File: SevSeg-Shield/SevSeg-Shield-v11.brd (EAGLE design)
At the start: 59.7 x 53.3 mm, 5 parts, among them U2 ARDUINO_SHIELD

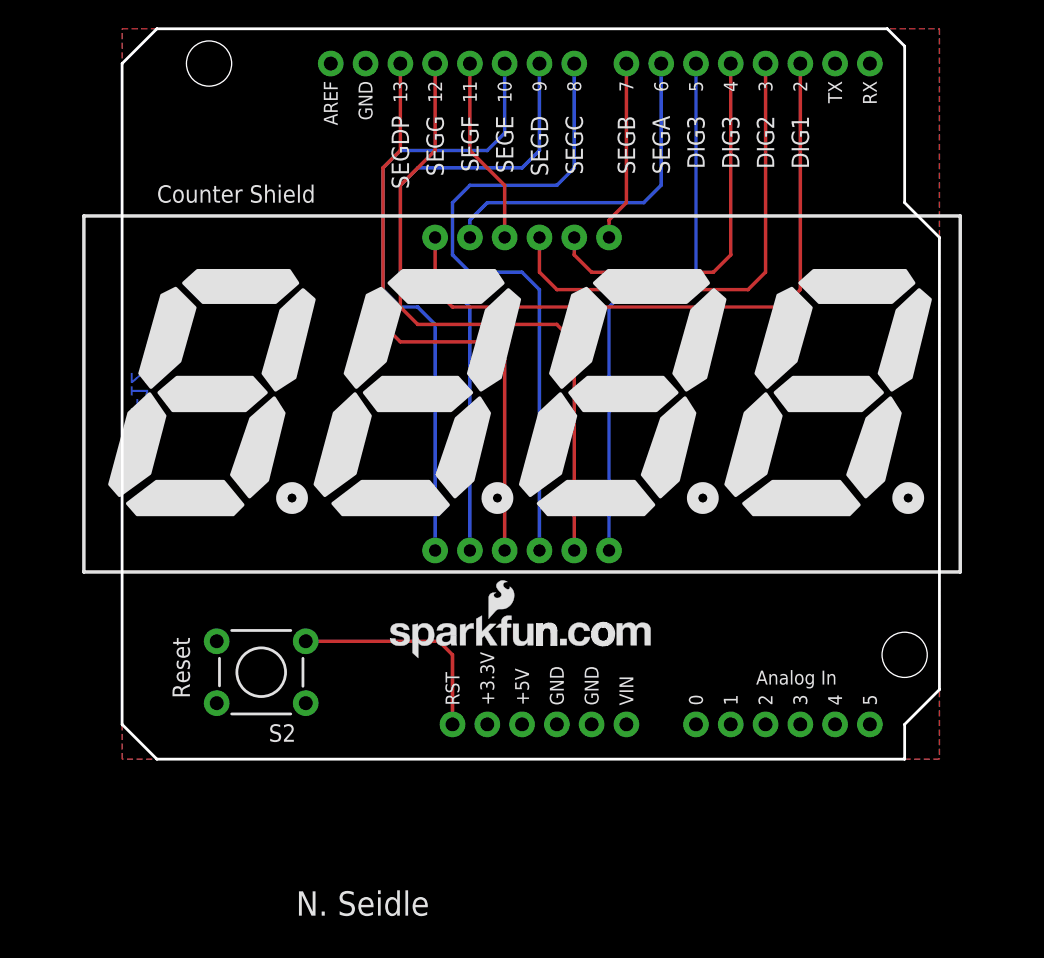
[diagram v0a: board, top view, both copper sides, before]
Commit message: Updated the footprint of the display.
Proto worked but the footprint was not quite right. This version should
work a lot better.
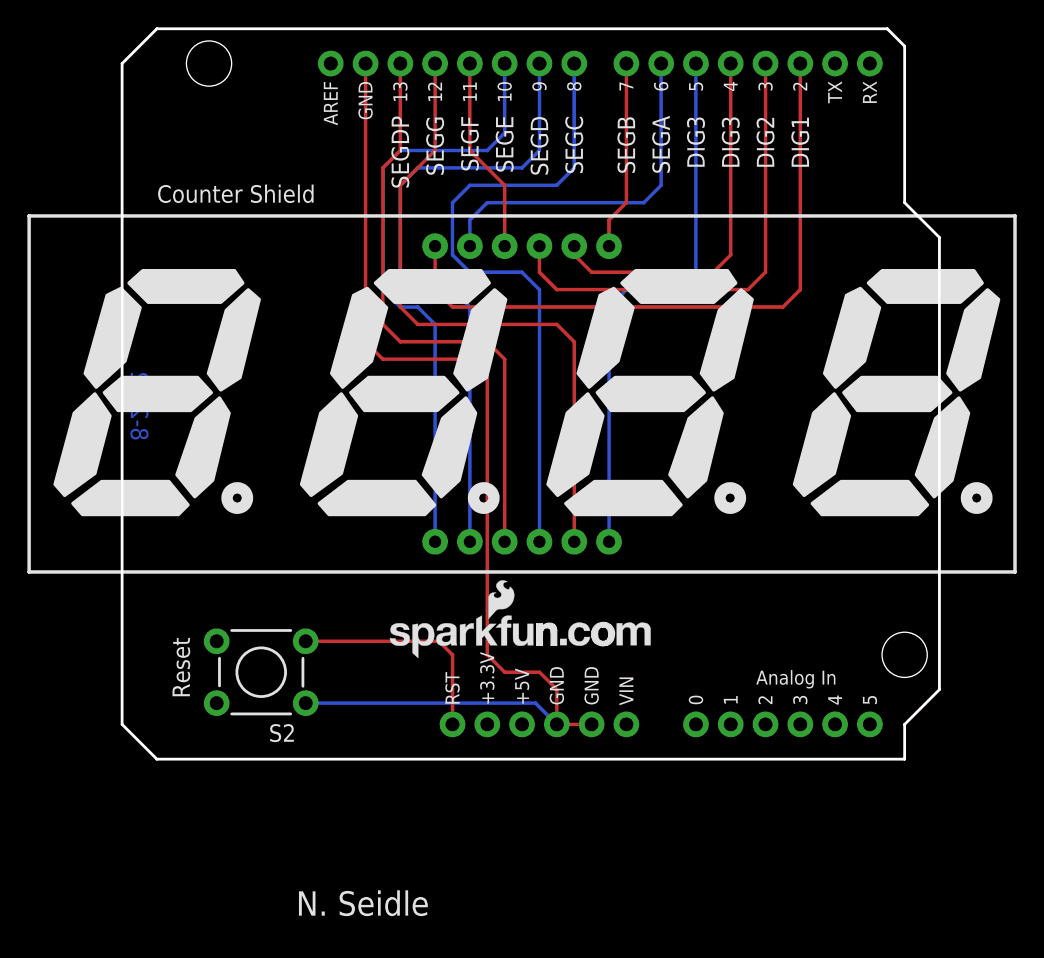
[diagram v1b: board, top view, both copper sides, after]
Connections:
- removed net VCC: U2.5V
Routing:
- net GND: track 0.00 -> 80.8 mm
- net SEGDP: track 43.5 -> 42.9 mm
- net SEGG: track 47.8 -> 47.2 mm
- net SEGF: track 13.8 -> 14.4 mm
- net SEGC: track 47.8 -> 47.2 mm
- net SEGB: track 13.2 -> 13.9 mm
- net SEGA: track 25.2 -> 25.8 mm
- net DIG3: track 27.7 -> 27.1 mm
- net DIG2: track 35.3 -> 34.7 mm
- net DIG1: track 48.0 -> 47.4 mm
- net SEGE: track 45.3 -> 44.6 mm
- net SEGD: track 47.8 -> 47.2 mm
- net DIG4: track 40.4 -> 39.8 mm
- removed copper zone on layer 1, net GND
- removed copper zone on layer 16, net GND
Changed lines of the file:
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@@
 <layer number="18" name="Vias" color="2" fill="1" visible="yes" active="yes"/>
 <layer number="19" name="Unrouted" color="6" fill="1" visible="yes" active="yes"/>
-<layer number="20" name="Dimension" color="6" fill="1" visible="yes" active="yes"/>
+<layer number="20" name="Dimension" color="24" fill="1" visible="yes" active="yes"/>
 <layer number="21" name="tPlace" color="16" fill="1" visible="yes" active="yes"/>
 <layer number="22" name="bPlace" color="14" fill="1" visible="yes" active="yes"/>
@@
 <contactref element="U2" pad="GND@0"/>
 <contactref element="S2" pad="1"/>
-<polygon width="0.2032" layer="1" isolate="0.3048">
-<vertex x="59.69" y="53.34"/>
-<vertex x="59.69" y="0"/>
-<vertex x="0" y="0"/>
-<vertex x="0" y="53.34"/>
-</polygon>
-<polygon width="0.2032" layer="16" isolate="0.3048">
-<vertex x="0" y="53.34"/>
-<vertex x="59.69" y="53.34"/>
-<vertex x="59.69" y="0"/>
-<vertex x="0" y="0"/>
-</polygon>
-</signal>
-<signal name="VCC">
-<contactref element="U2" pad="5V"/>
+<wire x1="17.78" y1="50.8" x2="17.78" y2="30.48" width="0.254" layer="1"/>
+<wire x1="17.78" y1="30.48" x2="19.05" y2="29.21" width="0.254" layer="1"/>
+<wire x1="19.05" y1="29.21" x2="25.4" y2="29.21" width="0.254" layer="1"/>
+<wire x1="25.4" y1="29.21" x2="26.67" y2="27.94" width="0.254" layer="1"/>
+<wire x1="26.67" y1="27.94" x2="26.67" y2="7.62" width="0.254" layer="1"/>
+<wire x1="26.67" y1="7.62" x2="27.94" y2="6.35" width="0.254" layer="1"/>
+<wire x1="27.94" y1="6.35" x2="30.48" y2="6.35" width="0.254" layer="1"/>
+<wire x1="30.48" y1="6.35" x2="31.75" y2="5.08" width="0.254" layer="1"/>
+<wire x1="31.75" y1="5.08" x2="31.75" y2="2.54" width="0.254" layer="1"/>
+<wire x1="13.4112" y1="4.0894" x2="30.2006" y2="4.0894" width="0.254" layer="16"/>
+<wire x1="30.2006" y1="4.0894" x2="31.75" y2="2.54" width="0.254" layer="16"/>
+<wire x1="34.29" y1="2.54" x2="31.75" y2="2.54" width="0.254" layer="1"/>
 </signal>
 <signal name="ARST">
@@
 <wire x1="48.26" y1="33.02" x2="24.13" y2="33.02" width="0.254" layer="1"/>
 <wire x1="24.13" y1="33.02" x2="22.86" y2="34.29" width="0.254" layer="1"/>
-<wire x1="22.86" y1="34.29" x2="22.86" y2="38.1" width="0.254" layer="1"/>
+<wire x1="22.86" y1="34.29" x2="22.86" y2="37.465" width="0.254" layer="1"/>
 </signal>
 <signal name="DIG2">
 <contactref element="U$1" pad="9"/>
 <contactref element="U2" pad="D3"/>
-<wire x1="30.48" y1="38.1" x2="30.48" y2="35.56" width="0.254" layer="1"/>
+<wire x1="30.48" y1="37.465" x2="30.48" y2="35.56" width="0.254" layer="1"/>
 <wire x1="30.48" y1="35.56" x2="31.75" y2="34.29" width="0.254" layer="1"/>
 <wire x1="31.75" y1="34.29" x2="45.72" y2="34.29" width="0.254" layer="1"/>
@@
 <contactref element="U$1" pad="8"/>
 <contactref element="U2" pad="D4"/>
-<wire x1="33.02" y1="38.1" x2="33.02" y2="36.83" width="0.254" layer="1"/>
+<wire x1="33.02" y1="37.465" x2="33.02" y2="36.83" width="0.254" layer="1"/>
 <wire x1="33.02" y1="36.83" x2="34.29" y2="35.56" width="0.254" layer="1"/>
 <wire x1="34.29" y1="35.56" x2="43.18" y2="35.56" width="0.254" layer="1"/>
@@
 <contactref element="U$1" pad="6"/>
 <contactref element="U2" pad="D5"/>
-<wire x1="35.56" y1="15.24" x2="35.56" y2="33.02" width="0.254" layer="16"/>
+<wire x1="35.56" y1="15.875" x2="35.56" y2="33.02" width="0.254" layer="16"/>
 <wire x1="35.56" y1="33.02" x2="36.83" y2="34.29" width="0.254" layer="16"/>
 <wire x1="36.83" y1="34.29" x2="40.64" y2="34.29" width="0.254" layer="16"/>
@@
 <contactref element="U$1" pad="3"/>
 <contactref element="U2" pad="D13"/>
-<wire x1="27.94" y1="15.24" x2="27.94" y2="29.21" width="0.254" layer="1"/>
+<wire x1="27.94" y1="15.875" x2="27.94" y2="29.21" width="0.254" layer="1"/>
 <wire x1="27.94" y1="29.21" x2="26.67" y2="30.48" width="0.254" layer="1"/>
 <wire x1="26.67" y1="30.48" x2="20.32" y2="30.48" width="0.254" layer="1"/>
@@
 <contactref element="U$1" pad="5"/>
 <contactref element="U2" pad="D12"/>
-<wire x1="33.02" y1="15.24" x2="33.02" y2="30.48" width="0.254" layer="1"/>
+<wire x1="33.02" y1="15.875" x2="33.02" y2="30.48" width="0.254" layer="1"/>
 <wire x1="33.02" y1="30.48" x2="31.75" y2="31.75" width="0.254" layer="1"/>
 <wire x1="31.75" y1="31.75" x2="21.59" y2="31.75" width="0.254" layer="1"/>
@@
 <contactref element="U$1" pad="10"/>
 <contactref element="U2" pad="D11"/>
-<wire x1="27.94" y1="38.1" x2="27.94" y2="41.91" width="0.254" layer="1"/>
+<wire x1="27.94" y1="37.465" x2="27.94" y2="41.91" width="0.254" layer="1"/>
 <wire x1="27.94" y1="41.91" x2="25.4" y2="44.45" width="0.254" layer="1"/>
 <wire x1="25.4" y1="44.45" x2="25.4" y2="50.8" width="0.254" layer="1"/>
@@
 <contactref element="U$1" pad="1"/>
 <contactref element="U2" pad="D10"/>
-<wire x1="22.86" y1="15.24" x2="22.86" y2="31.75" width="0.254" layer="16"/>
+<wire x1="22.86" y1="15.875" x2="22.86" y2="31.75" width="0.254" layer="16"/>
 <wire x1="19.05" y1="34.29" x2="19.05" y2="43.18" width="0.254" layer="16"/>
 <wire x1="19.05" y1="43.18" x2="20.32" y2="44.45" width="0.254" layer="16"/>
@@
 <contactref element="U$1" pad="2"/>
 <contactref element="U2" pad="D9"/>
-<wire x1="25.4" y1="15.24" x2="25.4" y2="33.02" width="0.254" layer="16"/>
+<wire x1="25.4" y1="15.875" x2="25.4" y2="33.02" width="0.254" layer="16"/>
 <wire x1="24.13" y1="34.29" x2="21.59" y2="34.29" width="0.254" layer="16"/>
 <wire x1="21.59" y1="34.29" x2="20.32" y2="35.56" width="0.254" layer="16"/>
@@
 <contactref element="U$1" pad="4"/>
 <contactref element="U2" pad="D8"/>
-<wire x1="30.48" y1="15.24" x2="30.48" y2="34.29" width="0.254" layer="16"/>
+<wire x1="30.48" y1="15.875" x2="30.48" y2="34.29" width="0.254" layer="16"/>
 <wire x1="30.48" y1="34.29" x2="29.21" y2="35.56" width="0.254" layer="16"/>
 <wire x1="29.21" y1="35.56" x2="25.4" y2="35.56" width="0.254" layer="16"/>
@@
 <contactref element="U$1" pad="7"/>
 <contactref element="U2" pad="D7"/>
-<wire x1="35.56" y1="38.1" x2="35.56" y2="39.37" width="0.254" layer="1"/>
+<wire x1="35.56" y1="37.465" x2="35.56" y2="39.37" width="0.254" layer="1"/>
 <wire x1="35.56" y1="39.37" x2="36.83" y2="40.64" width="0.254" layer="1"/>
 <wire x1="36.83" y1="40.64" x2="36.83" y2="50.8" width="0.254" layer="1"/>
@@
 <contactref element="U$1" pad="11"/>
 <contactref element="U2" pad="D6"/>
-<wire x1="25.4" y1="38.1" x2="25.4" y2="39.37" width="0.254" layer="16"/>
+<wire x1="25.4" y1="37.465" x2="25.4" y2="39.37" width="0.254" layer="16"/>
 <wire x1="25.4" y1="39.37" x2="26.67" y2="40.64" width="0.254" layer="16"/>
 <wire x1="26.67" y1="40.64" x2="38.1" y2="40.64" width="0.254" layer="16"/>
